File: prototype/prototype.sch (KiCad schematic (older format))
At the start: 33 parts, among them P1 CONN_25X2, P2 CONN_25X2, P3 VGACONN, U1 MC68SEC000

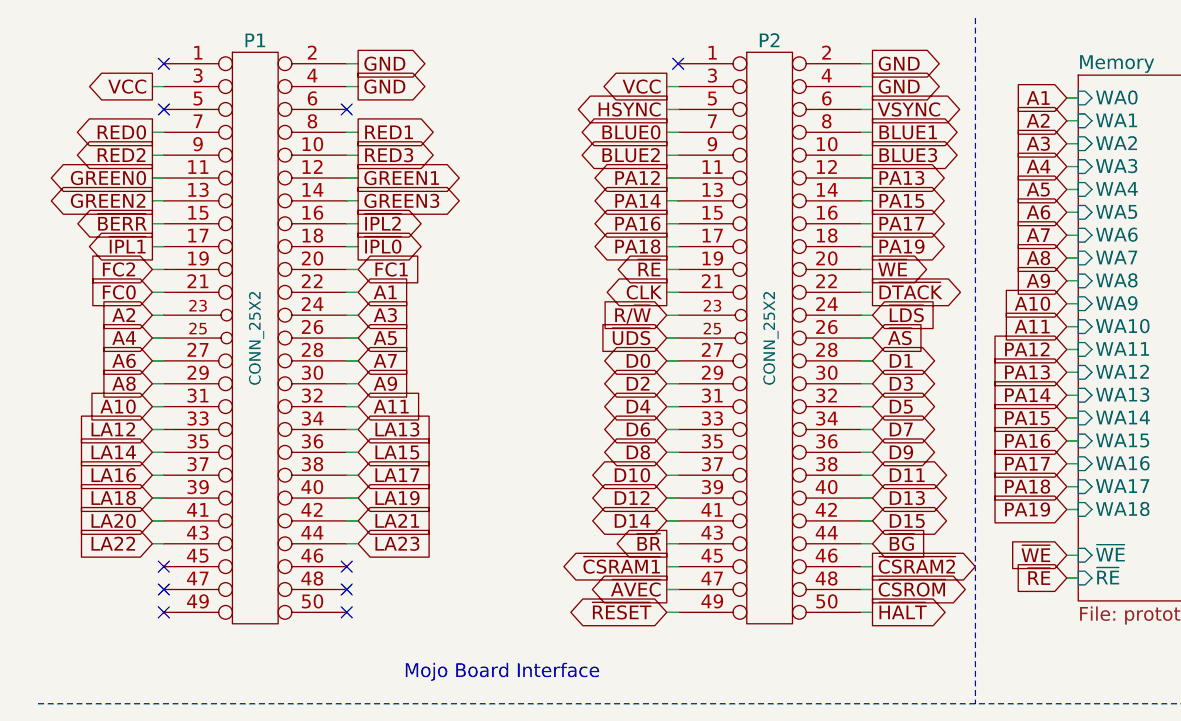
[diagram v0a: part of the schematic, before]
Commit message: Reassign mojo header pins to move VGA to the other end.
There is no room at the left-hand edge for the VGA connector because the
AVR header is in the way, so we need to move it to the right-hand edge.
To ease routing, the signals should therefore be exposed at that end too.
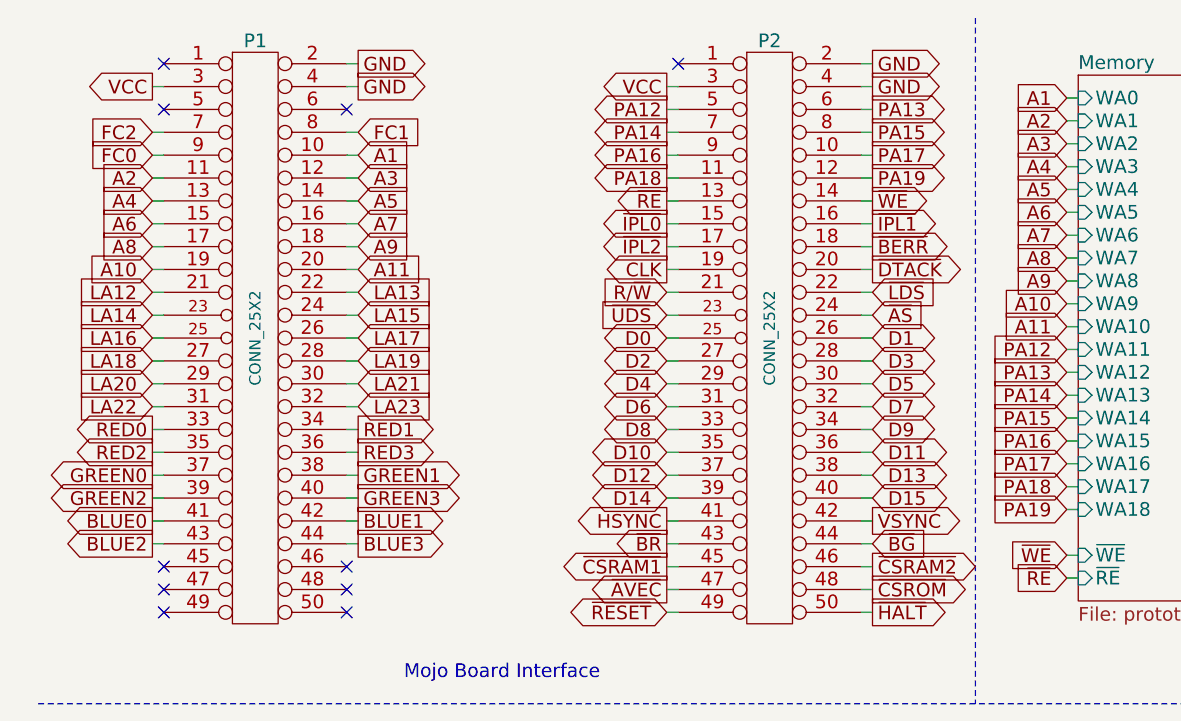
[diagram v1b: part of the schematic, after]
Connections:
- net A1: now also P1.10 (P10); no longer P1.22 (P22)
- net A10: now also P1.19 (P19); no longer P1.31 (P31)
- net A11: now also P1.20 (P20); no longer P1.32 (P32)
- net A2: now also P1.11 (P11); no longer P1.23 (P23)
- net A3: now also P1.12 (P12); no longer P1.24 (P24)
- net A4: now also P1.13 (P13); no longer P1.25 (P25)
- net A5: now also P1.14 (P14); no longer P1.26 (P26)
- net A6: now also P1.15 (P15); no longer P1.27 (P27)
- net A7: now also P1.16 (P16); no longer P1.28 (P28)
- net A8: now also P1.17 (P17); no longer P1.29 (P29)
- net A9: now also P1.18 (P18); no longer P1.30 (P30)
- net BLUE0: now also P1.41 (P41); no longer P2.7 (P7)
- net BLUE1: now also P1.42 (P42); no longer P2.8 (P8)
- net BLUE2: now also P1.43 (P43); no longer P2.9 (P9)
- net BLUE3: now also P1.44 (P44); no longer P2.10 (P10)
- net CLK: now also P2.19 (P19); no longer P2.21 (P21)
- net D0: now also P2.25 (P25); no longer P2.27 (P27)
- net D1: now also P2.26 (P26); no longer P2.28 (P28)
- net D10: now also P2.35 (P35); no longer P2.37 (P37)
- net D11: now also P2.36 (P36); no longer P2.38 (P38)
- net D12: now also P2.37 (P37); no longer P2.39 (P39)
- net D13: now also P2.38 (P38); no longer P2.40 (P40)
- net D14: now also P2.39 (P39); no longer P2.41 (P41)
- net D15: now also P2.40 (P40); no longer P2.42 (P42)
- net D2: now also P2.27 (P27); no longer P2.29 (P29)
- net D3: now also P2.28 (P28); no longer P2.30 (P30)
- net D4: now also P2.29 (P29); no longer P2.31 (P31)
- net D5: now also P2.30 (P30); no longer P2.32 (P32)
- net D6: now also P2.31 (P31); no longer P2.33 (P33)
- net D7: now also P2.32 (P32); no longer P2.34 (P34)
- net D8: now also P2.33 (P33); no longer P2.35 (P35)
- net D9: now also P2.34 (P34); no longer P2.36 (P36)
- net FC0: now also P1.9 (P9); no longer P1.21 (P21)
- net FC1: now also P1.8 (P8); no longer P1.20 (P20)
- net FC2: now also P1.7 (P7); no longer P1.19 (P19)
- net GREEN0: now also P1.37 (P37); no longer P1.11 (P11)
- net GREEN1: now also P1.38 (P38); no longer P1.12 (P12)
- net GREEN2: now also P1.39 (P39); no longer P1.13 (P13)
- net GREEN3: now also P1.40 (P40); no longer P1.14 (P14)
- net HSYNC: now also P2.41 (P41); no longer P2.5 (P5)
- net LA12: now also P1.21 (P21); no longer P1.33 (P33)
- net LA13: now also P1.22 (P22); no longer P1.34 (P34)
- net LA14: now also P1.23 (P23); no longer P1.35 (P35)
- net LA15: now also P1.24 (P24); no longer P1.36 (P36)
- net LA16: now also P1.25 (P25); no longer P1.37 (P37)
- net LA17: now also P1.26 (P26); no longer P1.38 (P38)
- net LA18: now also P1.27 (P27); no longer P1.39 (P39)
- net LA19: now also P1.28 (P28); no longer P1.40 (P40)
- net LA20: now also P1.29 (P29); no longer P1.41 (P41)
- net LA21: now also P1.30 (P30); no longer P1.42 (P42)
- net LA22: now also P1.31 (P31); no longer P1.43 (P43)
- net LA23: now also P1.32 (P32); no longer P1.44 (P44)
- net PA12: now also P2.5 (P5); no longer P2.11 (P11)
- net PA13: now also P2.6 (P6); no longer P2.12 (P12)
- net PA14: now also P2.7 (P7); no longer P2.13 (P13)
- net PA15: now also P2.8 (P8); no longer P2.14 (P14)
- net PA16: now also P2.9 (P9); no longer P2.15 (P15)
- net PA17: now also P2.10 (P10); no longer P2.16 (P16)
- net PA18: now also P2.11 (P11); no longer P2.17 (P17)
- net PA19: now also P2.12 (P12); no longer P2.18 (P18)
- net R/~W: now also P2.21 (P21); no longer P2.23 (P23)
- net RED0: now also P1.33 (P33); no longer P1.7 (P7)
- net RED1: now also P1.34 (P34); no longer P1.8 (P8)
- net RED2: now also P1.35 (P35); no longer P1.9 (P9)
- net RED3: now also P1.36 (P36); no longer P1.10 (P10)
- net VSYNC: now also P2.42 (P42); no longer P2.6 (P6)
- net ~AS: now also P2.24 (P24); no longer P2.26 (P26)
- net ~BERR: now also P2.18 (P18); no longer P1.15 (P15)
- net ~DTACK: now also P2.20 (P20); no longer P2.22 (P22)
- net ~IPL0: now also P2.15 (P15); no longer P1.18 (P18)
- net ~IPL1: now also P2.16 (P16); no longer P1.17 (P17)
- net ~IPL2: now also P2.17 (P17); no longer P1.16 (P16)
- net ~LDS: now also P2.22 (P22); no longer P2.24 (P24)
- net ~RE: now also P2.13 (P13); no longer P2.19 (P19)
- net ~UDS: now also P2.23 (P23); no longer P2.25 (P25)
- net ~WE: now also P2.14 (P14); no longer P2.20 (P20)

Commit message: Assign appropriate footprints to the memory ICs.
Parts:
- D1, D10, D2, D3, D4, D5, D6, D7, D8, D9: footprint Diodes_SMD:Diode_SOT23_Handsoldering -> 68k-computer:SOT-23_Diode
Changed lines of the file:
@@
 F 0 "D5" H 2400 4250 40  0000 C CNN
 F 1 "DIODE" H 2400 4050 40  0000 C CNN
-F 2 "Diodes_SMD:Diode_SOT23_Handsoldering" H 2400 4150 60  0001 C CNN
+F 2 "68k-computer:SOT-23_Diode" H 2400 4150 60  0001 C CNN
 F 3 "" H 2400 4150 60  0000 C CNN
 	1    2400 4150
@@
 F 0 "D8" H 2900 4250 40  0000 C CNN
 F 1 "DIODE" H 2900 4050 40  0000 C CNN
-F 2 "Diodes_SMD:Diode_SOT23_Handsoldering" H 2900 4150 60  0001 C CNN
+F 2 "68k-computer:SOT-23_Diode" H 2900 4150 60  0001 C CNN
 F 3 "" H 2900 4150 60  0000 C CNN
 	1    2900 4150
@@
 F 0 "D6" H 2400 5250 40  0000 C CNN
 F 1 "DIODE" H 2400 5050 40  0000 C CNN
-F 2 "Diodes_SMD:Diode_SOT23_Handsoldering" H 2400 5150 60  0001 C CNN
+F 2 "68k-computer:SOT-23_Diode" H 2400 5150 60  0001 C CNN
 F 3 "" H 2400 5150 60  0000 C CNN
 	1    2400 5150
@@
 F 0 "D9" H 2900 5250 40  0000 C CNN
 F 1 "DIODE" H 2900 5050 40  0000 C CNN
-F 2 "Diodes_SMD:Diode_SOT23_Handsoldering" H 2900 5150 60  0001 C CNN
+F 2 "68k-computer:SOT-23_Diode" H 2900 5150 60  0001 C CNN
 F 3 "" H 2900 5150 60  0000 C CNN
 	1    2900 5150
@@
 F 0 "D7" H 2400 6250 40  0000 C CNN
 F 1 "DIODE" H 2400 6050 40  0000 C CNN
-F 2 "Diodes_SMD:Diode_SOT23_Handsoldering" H 2400 6150 60  0001 C CNN
+F 2 "68k-computer:SOT-23_Diode" H 2400 6150 60  0001 C CNN
 F 3 "" H 2400 6150 60  0000 C CNN
 	1    2400 6150
@@
 F 0 "D10" H 2900 6250 40  0000 C CNN
 F 1 "DIODE" H 2900 6050 40  0000 C CNN
-F 2 "Diodes_SMD:Diode_SOT23_Handsoldering" H 2900 6150 60  0001 C CNN
+F 2 "68k-computer:SOT-23_Diode" H 2900 6150 60  0001 C CNN
 F 3 "" H 2900 6150 60  0000 C CNN
 	1    2900 6150
@@
 F 0 "D2" H 1250 7500 40  0000 C CNN
 F 1 "DIODE" H 1250 7300 40  0000 C CNN
-F 2 "Diodes_SMD:Diode_SOT23_Handsoldering" H 1250 7400 60  0001 C CNN
+F 2 "68k-computer:SOT-23_Diode" H 1250 7400 60  0001 C CNN
 F 3 "" H 1250 7400 60  0000 C CNN
 	1    1250 7400
@@
 F 0 "D1" H 1250 7000 40  0000 C CNN
 F 1 "DIODE" H 1250 6800 40  0000 C CNN
-F 2 "Diodes_SMD:Diode_SOT23_Handsoldering" H 1250 6900 60  0001 C CNN
+F 2 "68k-computer:SOT-23_Diode" H 1250 6900 60  0001 C CNN
 F 3 "" H 1250 6900 60  0000 C CNN
 	1    1250 6900
@@
 F 0 "D4" H 2200 7500 40  0000 C CNN
 F 1 "DIODE" H 2200 7300 40  0000 C CNN
-F 2 "Diodes_SMD:Diode_SOT23_Handsoldering" H 2200 7400 60  0001 C CNN
+F 2 "68k-computer:SOT-23_Diode" H 2200 7400 60  0001 C CNN
 F 3 "" H 2200 7400 60  0000 C CNN
 	1    2200 7400
@@
 F 0 "D3" H 2200 7000 40  0000 C CNN
 F 1 "DIODE" H 2200 6800 40  0000 C CNN
-F 2 "Diodes_SMD:Diode_SOT23_Handsoldering" H 2200 6900 60  0001 C CNN
+F 2 "68k-computer:SOT-23_Diode" H 2200 6900 60  0001 C CNN
 F 3 "" H 2200 6900 60  0000 C CNN
 	1    2200 6900

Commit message: PCB floor planning.
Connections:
- net HSYNC: now also D1.1 (A), D2.2 (K)
- net VCC: now also D1.2 (K), D3.2 (K); no longer D1.1 (A), D3.1 (A)
- net VSYNC: now also D3.1 (A), D4.2 (K)
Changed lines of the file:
@@
 	2650 4500 2750 4500
 Connection ~ 2650 4350
-Text GLabel 750  7150 2    60   Output ~ 0
+Text GLabel 1100 7150 0    60   Input ~ 0
 HSYNC
 $Comp
@@
 F 3 "" H 1250 6900 60  0000 C CNN
 	1    1250 6900
-	0    1    1    0
+	0    -1   -1   0
 $EndComp
 Wire Wire Line
 	1250 7100 1250 7200
-Wire Wire Line
-	1100 7150 1250 7150
 Connection ~ 1250 7150
 $Comp
@@
 Wire Wire Line
 	1250 7600 1250 7650
-Text GLabel 1700 7150 2    60   Output ~ 0
+Text GLabel 2050 7150 0    60   Input ~ 0
 VSYNC
 $Comp
@@
 F 3 "" H 2200 6900 60  0000 C CNN
 	1    2200 6900
-	0    1    1    0
+	0    -1   -1   0
 $EndComp
 Wire Wire Line
 	2200 7100 2200 7200
-Wire Wire Line
-	2050 7150 2200 7150
 Connection ~ 2200 7150
 $Comp
@@
 Wire Wire Line
 	3350 1500 3400 1500
+Wire Wire Line
+	2050 7150 2200 7150
+Wire Wire Line
+	1100 7150 1250 7150
 $EndSCHEMATC

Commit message: "Rescue" the schematic after a KiCad upgrade.
Some symbols changed in the new version.
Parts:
- C1, C2, C3, C4: symbol C -> C-RESCUE-prototype
- R1, R10, R11, R12, R13, R14, R15, R2, R3, R4, R5, R6, R7, R8, R9: symbol R -> R-RESCUE-prototype
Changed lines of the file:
@@
 EESchema Schematic File Version 2
+LIBS:prototype-rescue
 LIBS:power
 LIBS:device
@@
 LIBS:memory
 LIBS:xilinx
-LIBS:special
 LIBS:microcontrollers
 LIBS:dsp
@@
 $EndComp
 $Comp
-L GND #PWR02
+L GND-RESCUE-prototype #PWR02
 U 1 1 5518ED53
 P 6650 7600
@@
 $EndComp
 $Comp
-L GND #PWR04
+L GND-RESCUE-prototype #PWR04
 U 1 1 5518EFE0
 P 9400 4950
@@
 ~RESET
 $Comp
-L R R1
+L R-RESCUE-prototype R1
 U 1 1 55190758
 P 10600 3500
@@
 $EndComp
 $Comp
-L C C2
+L C-RESCUE-prototype C2
 U 1 1 5519107D
 P 9250 5750
@@
 $EndComp
 $Comp
-L C C3
+L C-RESCUE-prototype C3
 U 1 1 551910BD
 P 9550 5750
@@
 $EndComp
 $Comp
-L C C4
+L C-RESCUE-prototype C4
 U 1 1 55191170
 P 9850 5750
@@
 $EndComp
 $Comp
-L C C1
+L C-RESCUE-prototype C1
 U 1 1 5519119C
 P 8950 5750
@@
 $EndComp
 $Comp
-L GND #PWR07
+L GND-RESCUE-prototype #PWR07
 U 1 1 551911E5
 P 9400 6150
@@
 RED0
 $Comp
-L R R2
+L R-RESCUE-prototype R2
 U 1 1 551926CF
 P 1450 3750
@@
 RED3
 $Comp
-L R R3
+L R-RESCUE-prototype R3
 U 1 1 551928F7
 P 1450 3950
@@
 $EndComp
 $Comp
-L R R4
+L R-RESCUE-prototype R4
 U 1 1 55192923
 P 1450 4150
@@
 $EndComp
 $Comp
-L R R5
+L R-RESCUE-prototype R5
 U 1 1 55192951
 P 1450 4350
@@
 $EndComp
 $Comp
-L GND #PWR08
+L GND-RESCUE-prototype #PWR08
 U 1 1 5519346A
 P 2150 4150
@@
 GREEN0
 $Comp
-L R R6
+L R-RESCUE-prototype R6
 U 1 1 55193CFF
 P 1450 4750
@@
 GREEN3
 $Comp
-L R R7
+L R-RESCUE-prototype R7
 U 1 1 55193D08
 P 1450 4950
@@
 $EndComp
 $Comp
-L R R8
+L R-RESCUE-prototype R8
 U 1 1 55193D0E
 P 1450 5150
@@
 $EndComp
 $Comp
-L R R9
+L R-RESCUE-prototype R9
 U 1 1 55193D14
 P 1450 5350
@@
 $EndComp
 $Comp
-L GND #PWR010
+L GND-RESCUE-prototype #PWR010
 U 1 1 55193D31
 P 2150 5150
@@
 BLUE0
 $Comp
-L R R10
+L R-RESCUE-prototype R10
 U 1 1 551940F6
 P 1450 5750
@@
 BLUE3
 $Comp
-L R R11
+L R-RESCUE-prototype R11
 U 1 1 551940FF
 P 1450 5950
@@
 $EndComp
 $Comp
-L R R12
+L R-RESCUE-prototype R12
 U 1 1 55194105
 P 1450 6150
@@
 $EndComp
 $Comp
-L R R13
+L R-RESCUE-prototype R13
 U 1 1 5519410B
 P 1450 6350
@@
 $EndComp
 $Comp
-L GND #PWR012
+L GND-RESCUE-prototype #PWR012
 U 1 1 55194128
 P 2150 6150
@@
 $EndComp
 $Comp
-L GND #PWR015
+L GND-RESCUE-prototype #PWR015
 U 1 1 55196080
 P 1250 7650
@@
 $EndComp
 $Comp
-L GND #PWR017
+L GND-RESCUE-prototype #PWR017
 U 1 1 5519643E
 P 2200 7650
@@
 VSYNC
 $Comp
-L GND #PWR018
+L GND-RESCUE-prototype #PWR018
 U 1 1 55196C8F
 P 4550 6100
@@
 	4550 6000 4650 6000
 $Comp
-L GND #PWR019
+L GND-RESCUE-prototype #PWR019
 U 1 1 5519790D
 P 5450 3950
@@
 	5450 4000 5450 3950
 $Comp
-L GND #PWR020
+L GND-RESCUE-prototype #PWR020
 U 1 1 55197AE6
 P 5450 6350
@@
 	7200 2600 7250 2600
 $Comp
-L R R14
+L R-RESCUE-prototype R14
 U 1 1 551C66AB
 P 4200 4700
@@
 $EndComp
 $Comp
-L R R15
+L R-RESCUE-prototype R15
 U 1 1 551C678E
 P 4200 4850
